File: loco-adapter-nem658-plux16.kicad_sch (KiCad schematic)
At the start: 1 part

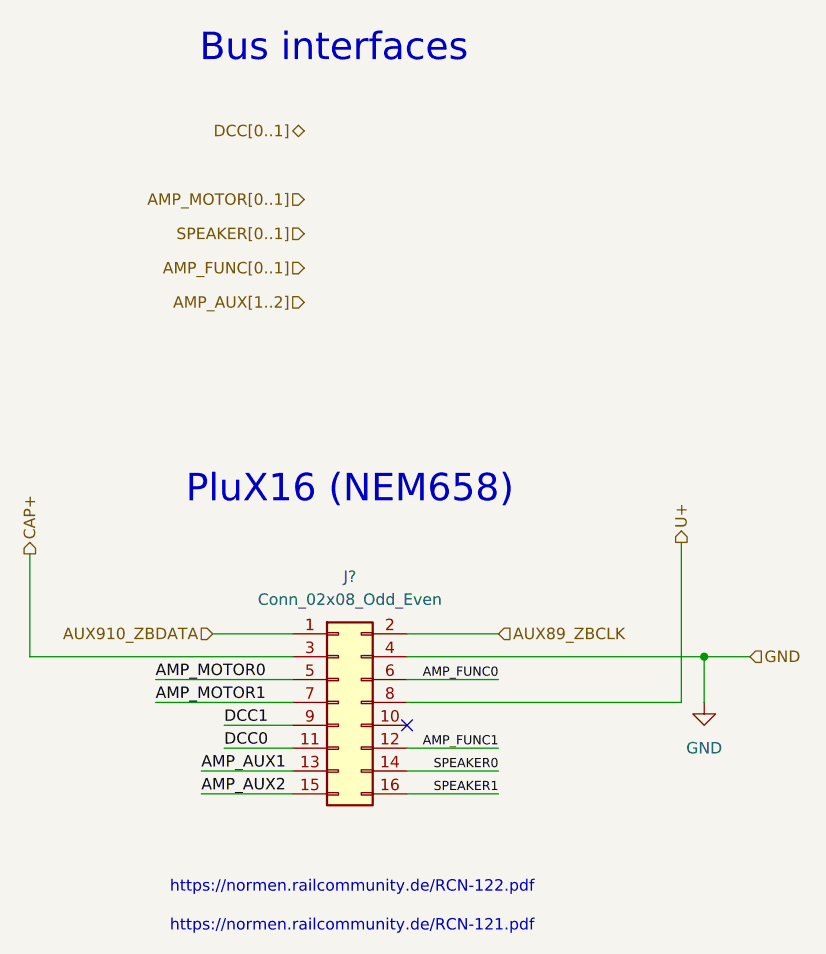
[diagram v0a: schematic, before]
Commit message: Add - New annotations of schematics
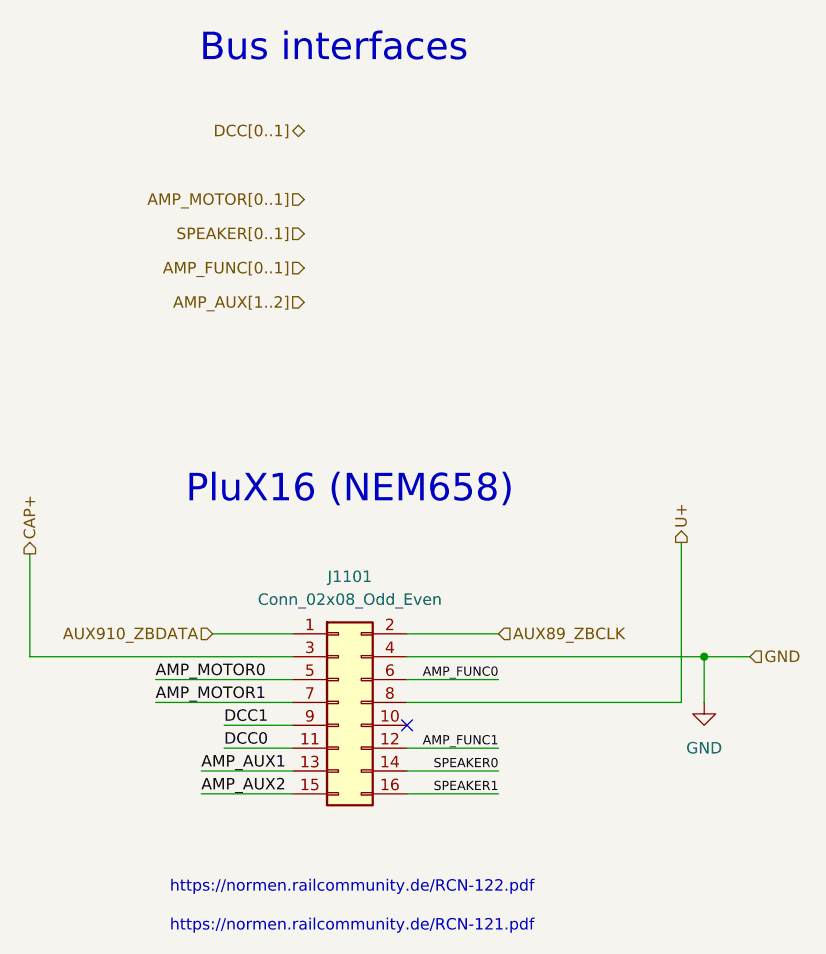
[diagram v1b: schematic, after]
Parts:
- gave numbers to parts that had none: 1
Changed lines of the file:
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@@
 			(project "xDuinoRails-Thor-M"
 				(path "/fb33ec4e-6596-45d2-a121-8d3475acd69a/3c699e35-5808-46af-b922-4c3eb1f6da5c/072872c0-59aa-4b8b-8887-ebeae887efaf"
-					(reference "#PWR?")
+					(reference "#PWR1101")
 					(unit 1)
 				)
@@
 		(dnp no)
 		(fields_autoplaced yes)
-		(property "Reference" "J?"
+		(property "Reference" "J1101"
 			(at 59.69 82.55 0)
 			(effects
@@
 			(project "xDuinoRails-Thor-M"
 				(path "/fb33ec4e-6596-45d2-a121-8d3475acd69a/3c699e35-5808-46af-b922-4c3eb1f6da5c/072872c0-59aa-4b8b-8887-ebeae887efaf"
-					(reference "J?")
+					(reference "J1101")
 					(unit 1)
 				)

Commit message: Add - Plux16 partnumber
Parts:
- J1101: OLI_ID (none) -> Plux16_02x08_1.27
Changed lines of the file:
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@@
+			)
+		)
+		(property "OLI_ID" "Plux16_02x08_1.27"
+			(at 58.42 96.52 0)
+			(effects
+				(font
+					(size 1.27 1.27)
+				)
+				(hide yes)
 			)
 		)
